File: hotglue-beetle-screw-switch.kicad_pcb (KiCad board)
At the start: 2 copper layers, 28 x 20 mm, 11 parts, among them J1 Conn_01x02_Pin, J2 Conn_01x02_Socket, J3 Conn_01x02_Socket, J4 Conn_01x02_Socket

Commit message: updated pcb with open solder mask for high current areas and cool looking text.
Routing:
- net -BATT: track 0.00 -> 2.09 mm
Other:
- board text added: "+"
- board text added: "-"
- board text added: "HOT GLUE"
- board text added: "V1.0"

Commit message: plotted gerbers for intial design. Began fix for incorrect footprint on Wurth standoff. Backup after PC crash and recovery
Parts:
- H2, H3: footprint Mounting_Wuerth:Mounting_Wuerth_WA-SMSI-M3_H3mm_9774030360 -> Trent-footprints:MP_Wurth_WP-SMBU_746600330

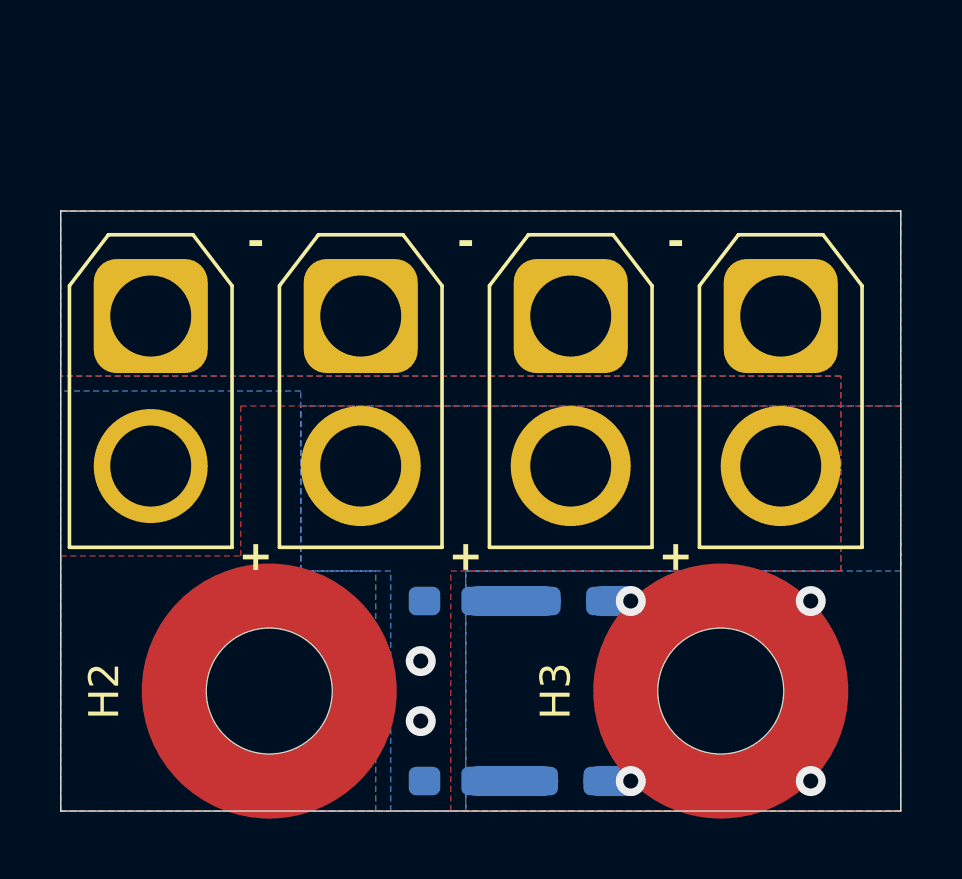
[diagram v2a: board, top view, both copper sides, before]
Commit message: overrode errors due to Wurth footprint library. Updated layout for larger hole size. updated gerbers.
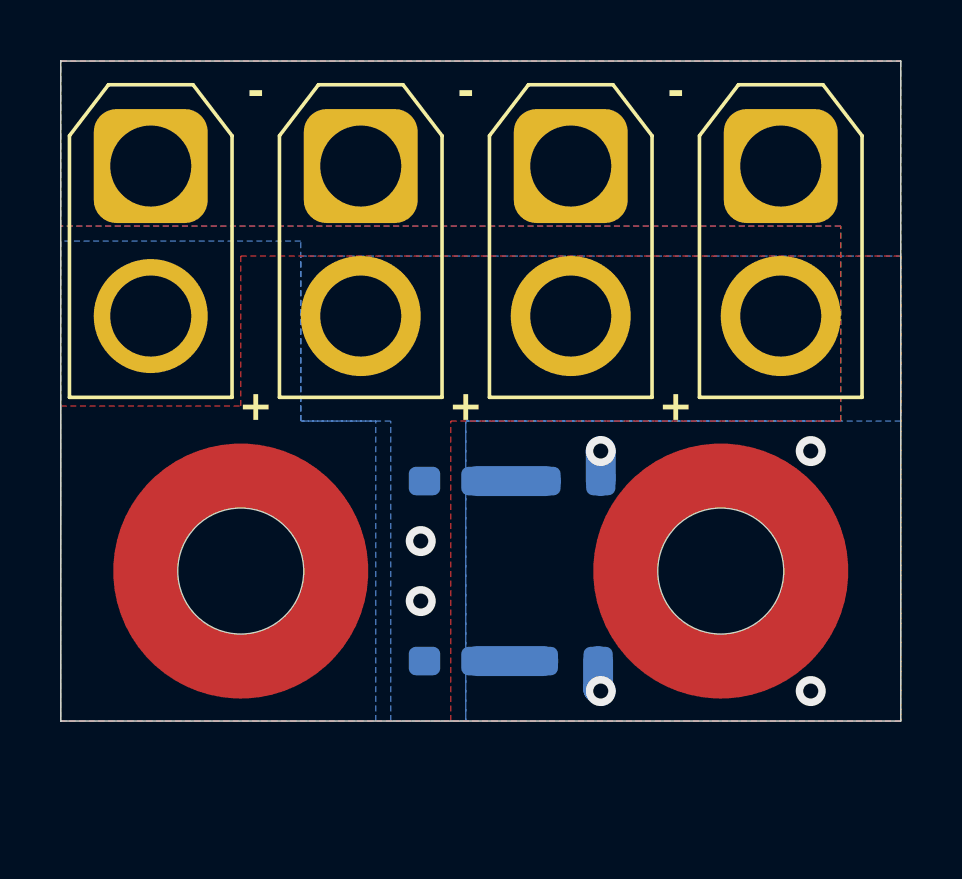
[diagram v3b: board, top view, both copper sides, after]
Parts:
- moved J1 5.00 mm to (103.0, 78.5)
- moved J2 5.00 mm to (110.0, 78.5)
- moved J3 5.00 mm to (117.0, 78.5)
- moved J4 5.00 mm to (124.0, 78.5)
- moved H1 4.11 mm to (106.0, 92.0)
- moved H2 4.11 mm to (106.0, 92.0)
- moved D1 4.00 mm to (113.0, 95.0)
- moved D2 4.00 mm to (113.0, 89.0)
- moved H3 4.00 mm to (122.0, 92.0)
- moved R1 4.00 mm to (117.0, 95.0)
- moved R2 4.00 mm to (117.1, 89.0)
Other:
- board size 28 x 20 mm -> 28 x 22 mm
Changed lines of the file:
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@@
 		(capping no)
 		(filling no)
-		(grid_origin 100 100)
+		(grid_origin 100 97)
 		(pcbplotparams
 			(layerselection 0x00000000_00000000_55555555_5755f5ff)
@@
 			(outputformat 1)
 			(mirror no)
-			(drillshape 1)
+			(drillshape 0)
 			(scaleselection 1)
-			(outputdirectory "")
+			(outputdirectory "Gerbers/")
 		)
 	)
 	(footprint "Trent-footprints:MP_Wurth_WP-SMBU_746600330"
 		(layer "F.Cu")
-		(at 122 96 90)
+		(at 122 92 90)
 		(descr "REDCUBE SMT with internal through-hole thread, body 7x7x3mm, https://www.we-online.com/en/components/products/datasheet/746600330?ki")
 		(tags "SMD")
@@
 			(unlocked yes)
 			(layer "F.SilkS")
+			(hide yes)
 			(effects
 				(font
@@
 	(footprint "Connector_AMASS:AMASS_XT30U-F_1x02_P5.0mm_Vertical"
 		(layer "F.Cu")
-		(at 110 83.5 -90)
+		(at 110 78.5 -90)
 		(descr "Connector XT30 Vertical Cable Female, https://www.tme.eu/Document/f2d0830114aabe6ea8d4bb128e962790/XT30U-F.pdf")
 		(tags "RC Connector XT30")
@@
 			(at 2.5 4 90)
 			(layer "F.Fab")
+			(hide yes)
 			(effects
 				(font
@@
 	(footprint "Connector_AMASS:AMASS_XT30U-M_1x02_P5.0mm_Vertical"
 		(layer "F.Cu")
-		(at 103 83.5 -90)
+		(at 103 78.5 -90)
 		(descr "Connector XT30 Vertical Cable Male, https://www.tme.eu/Document/7d9d972ae3468777f69ec2ee99897652/XT30U-M.pdf")
 		(tags "RC Connector XT30")
@@
 			(at 2.5 4 90)
 			(layer "F.Fab")
+			(hide yes)
 			(effects
 				(font
@@
 	(footprint "Connector_AMASS:AMASS_XT30U-F_1x02_P5.0mm_Vertical"
 		(layer "F.Cu")
-		(at 117 83.5 -90)
+		(at 117 78.5 -90)
 		(descr "Connector XT30 Vertical Cable Female, https://www.tme.eu/Document/f2d0830114aabe6ea8d4bb128e962790/XT30U-F.pdf")
 		(tags "RC Connector XT30")
@@
 			(at 2.5 4 90)
 			(layer "F.Fab")
+			(hide yes)
 			(effects
 				(font
@@
 	(footprint "Trent-footprints:MP_Wurth_WP-SMBU_746600330"
 		(layer "F.Cu")
-		(at 106.95 96 90)
+		(at 106 92 90)
 		(descr "REDCUBE SMT with internal through-hole thread, body 7x7x3mm, https://www.we-online.com/en/components/products/datasheet/746600330?ki")
 		(tags "SMD")
@@
 			(unlocked yes)
 			(layer "F.SilkS")
+			(hide yes)
 			(effects
 				(font
@@
 	(footprint "Connector_AMASS:AMASS_XT30U-F_1x02_P5.0mm_Vertical"
 		(layer "F.Cu")
-		(at 124 83.5 -90)
+		(at 124 78.5 -90)
 		(descr "Connector XT30 Vertical Cable Female, https://www.tme.eu/Document/f2d0830114aabe6ea8d4bb128e962790/XT30U-F.pdf")
 		(tags "RC Connector XT30")
@@
 			(at 2.5 4 90)
 			(layer "F.Fab")
+			(hide yes)
 			(effects
 				(font
@@
 	(footprint "Resistor_SMD:R_0603_1608Metric_Pad0.98x0.95mm_HandSolder"
 		(layer "B.Cu")
-		(at 117 99)
+		(at 117 95)
 		(descr "Resistor SMD 0603 (1608 Metric), square (rectangular) end terminal, IPC-7351 nominal with elongated pad for handsoldering. (Body size source: IPC-SM-782 page 72, https://www.pcb-3d.com/wordpress/wp-content/uploads/ipc-sm-782a_amendment_1_and_2.pdf)")
 		(tags "resistor handsolder")
@@
 	(footprint "Resistor_SMD:R_0603_1608Metric_Pad0.98x0.95mm_HandSolder"
 		(layer "B.Cu")
-		(at 117.0875 93)
+		(at 117.0875 89)
 		(descr "Resistor SMD 0603 (1608 Metric), square (rectangular) end terminal, IPC-7351 nominal with elongated pad for handsoldering. (Body size source: IPC-SM-782 page 72, https://www.pcb-3d.com/wordpress/wp-content/uploads/ipc-sm-782a_amendment_1_and_2.pdf)")
 		(tags "resistor handsolder")
@@
 	(footprint "Diode_SMD:D_0603_1608Metric_Pad1.05x0.95mm_HandSolder"
 		(layer "B.Cu")
-		(at 113 93 180)
+		(at 113 89 180)
 		(descr "Diode SMD 0603 (1608 Metric), square (rectangular) end terminal, IPC-7351 nominal, (Body size source: http://www.tortai-tech.com/upload/download/2011102023233369053.pdf)")
 		(tags "diode handsolder")
@@
 	(footprint "Trent-footprints:Wurth-M3-screw-contact"
 		(layer "B.Cu")
-		(at 106.95 96 180)
+		(at 106 92 180)
 		(descr "Mounting Hardware, inside through hole M3, height 3, Wuerth electronics 9774030360 (https://www.we-online.com/components/products/datasheet/9774030360R.pdf)")
 		(tags "Mounting M3 9774030360")
@@
 			(at 0 -4.65 0)
 			(layer "B.Fab")
+			(hide yes)
 			(effects
 				(font
@@
 	(footprint "Diode_SMD:D_0603_1608Metric_Pad1.05x0.95mm_HandSolder"
 		(layer "B.Cu")
-		(at 113 99 180)
+		(at 113 95 180)
 		(descr "Diode SMD 0603 (1608 Metric), square (rectangular) end terminal, IPC-7351 nominal, (Body size source: http://www.tortai-tech.com/upload/download/2011102023233369053.pdf)")
 		(tags "diode handsolder")
@@
 	)
 	(gr_rect
-		(start 100 80)
-		(end 128 100)
+		(start 100 75)
+		(end 128 97)
 		(stroke
 			(width 0.05)
@@
 	)
 	(gr_text "HOT\nGLUE"
-		(at 115.5 96 0)
+		(at 115.5 91 0)
 		(layer "F.Mask")
 		(effects
@@
 	)
 	(gr_text "V1.0"
-		(at 115.5 96 0)
+		(at 115.5 92 0)
 		(layer "B.Mask")
 		(effects
@@
 	)
 	(gr_text "-"
-		(at 106.5 81 0)
+		(at 106.5 76 0)
 		(layer "F.SilkS")
 		(effects
@@
 	)
 	(gr_text "+"
-		(at 106.5 91.5 0)
+		(at 106.5 86.5 0)
 		(layer "F.SilkS")
 		(effects
@@
 	)
 	(gr_text "-"
-		(at 113.5 81 0)
+		(at 113.5 76 0)
 		(layer "F.SilkS")
 		(effects
@@
 	)
 	(gr_text "+"
-		(at 113.5 91.5 0)
+		(at 113.5 86.5 0)
 		(layer "F.SilkS")
 		(effects
@@
 	)
 	(gr_text "-"
-		(at 120.5 81 0)
+		(at 120.5 76 0)
 		(layer "F.SilkS")
 		(effects
@@
 	)
 	(gr_text "+"
-		(at 120.5 91.5 0)
+		(at 120.5 86.5 0)
 		(layer "F.SilkS")
 		(effects
@@
 	)
 	(gr_text "-"
-		(at 106.5 81 0)
+		(at 106.5 76 0)
 		(layer "B.SilkS")
 		(effects
@@
 	)
 	(gr_text "+"
-		(at 106.5 88 0)
+		(at 106.5 83 0)
 		(layer "B.SilkS")
 		(effects
@@
 	)
 	(gr_text "-"
-		(at 113.5 81 0)
+		(at 113.5 76 0)
 		(layer "B.SilkS")
 		(effects
@@
 	)
 	(gr_text "+"
-		(at 113.5 91.5 0)
+		(at 113.5 86.5 0)
 		(layer "B.SilkS")
 		(effects
@@
 	)
 	(gr_text "-"
-		(at 120.5 81 0)
+		(at 120.5 76 0)
 		(layer "B.SilkS")
 		(effects
@@
 	)
 	(gr_text "+"
-		(at 120.5 91.5 0)
+		(at 120.5 86.5 0)
 		(layer "B.SilkS")
 		(effects
@@
 	)
 	(via
-		(at 119 99)
+		(at 118 96)
 		(size 1)
 		(drill 0.5)
@@
 	)
 	(via
-		(at 119 93)
+		(at 118 88)
 		(size 1)
 		(drill 0.5)
@@
 	)
 	(via
-		(at 125 99)
+		(at 125 96)
 		(size 1)
 		(drill 0.5)
@@
 	)
 	(via
-		(at 125 93)
+		(at 125 88)
 		(size 1)
 		(drill 0.5)
@@
 	)
 	(segment
-		(start 117.9125 99)
-		(end 119 99)
+		(start 118 89)
+		(end 118 88)
+		(width 1)
+		(layer "B.Cu")
+		(net "-BATT")
+	)
+	(segment
+		(start 117.9125 95.9125)
+		(end 118 96)
 		(width 1)
 		(layer "B.Cu")
@@
 	)
 	(segment
-		(start 118 93)
-		(end 119 93)
+		(start 117.9125 95)
+		(end 117.9125 95.9125)
 		(width 1)
 		(layer "B.Cu")
@@
 	)
 	(via
-		(at 112 95)
+		(at 112 91)
 		(size 1)
 		(drill 0.5)
@@
 	)
 	(via
-		(at 112 97)
+		(at 112 93)
 		(size 1)
 		(drill 0.5)
@@
 	)
 	(segment
-		(start 113.875 99)
-		(end 116.0875 99)
+		(start 113.875 95)
+		(end 116.0875 95)
 		(width 1)
 		(layer "B.Cu")
@@
 	)
 	(segment
-		(start 113.875 93)
-		(end 116.175 93)
+		(start 113.875 89)
+		(end 116.175 89)
 		(width 1)
 		(layer "B.Cu")
@@
 		(polygon
 			(pts
-				(xy 100 80) (xy 128 80) (xy 128 100) (xy 113 100) (xy 113 92) (xy 126 92) (xy 126 85.5) (xy 100 85.5)
+				(xy 100 75) (xy 128 75) (xy 128 97) (xy 113 97) (xy 113 87) (xy 126 87) (xy 126 80.5) (xy 100 80.5)
 			)
 		)
@@
 		(polygon
 			(pts
-				(xy 128 86.5) (xy 128 92) (xy 128 100) (xy 100 100) (xy 100 91.5) (xy 106 91.5) (xy 106 86.5)
+				(xy 128 81.5) (xy 128 87) (xy 128 97) (xy 100 97) (xy 100 86.5) (xy 106 86.5) (xy 106 81.5)
 			)
 		)
@@
 		(polygon
 			(pts
-				(xy 100 86) (xy 100 100) (xy 110.5 100) (xy 110.5 92) (xy 108 92) (xy 108 86)
+				(xy 100 81) (xy 100 97) (xy 110.5 97) (xy 110.5 87) (xy 108 87) (xy 108 81)
 			)
 		)
@@
 		(polygon
 			(pts
-				(xy 111 100) (xy 111 92) (xy 108 92) (xy 108 86.5) (xy 128 86.5) (xy 128 92) (xy 113.5 92) (xy 113.5 100)
+				(xy 111 97) (xy 111 87) (xy 108 87) (xy 108 81.5) (xy 128 81.5) (xy 128 87) (xy 113.5 87) (xy 113.5 97)
 			)
 		)
@@
 		(polygon
 			(pts
-				(xy 128 84.5) (xy 128 91) (xy 128 100) (xy 113.5 100) (xy 113.5 92) (xy 126 92) (xy 126 85.5) (xy 100 85.5)
-				(xy 100 80) (xy 128 80)
+				(xy 128 79.5) (xy 128 86) (xy 128 97) (xy 113.5 97) (xy 113.5 87) (xy 126 87) (xy 126 80.5) (xy 100 80.5)
+				(xy 100 75) (xy 128 75)
 			)
 		)
@@
 		(polygon
 			(pts
-				(xy 101.5 85.5) (xy 125.5 85.5) (xy 125.5 81.5) (xy 101.5 81.5)
+				(xy 101.5 80.5) (xy 125.5 80.5) (xy 125.5 76.5) (xy 101.5 76.5)
 			)
 		)
@@
 		(polygon
 			(pts
-				(xy 101 86.5) (xy 101 90.5) (xy 104 99.5) (xy 108 99.5) (xy 108 92.5) (xy 105 86.5)
+				(xy 101 81.5) (xy 101 85.5) (xy 104 94.5) (xy 106 94.5) (xy 106 83.5) (xy 105 81.5)
 			)
 		)
@@
 		(polygon
 			(pts
-				(xy 108.5 86.5) (xy 125.5 86.5) (xy 125.5 90.5) (xy 108.5 90.5)
+				(xy 108.5 81.5) (xy 125.5 81.5) (xy 125.5 85.5) (xy 108.5 85.5)
 			)
 		)
